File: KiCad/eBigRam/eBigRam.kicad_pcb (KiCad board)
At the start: 2 copper layers, 101.6 x 50.8 mm, 8 parts, among them J1 Conn_02x20_Counter_Clockwise_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

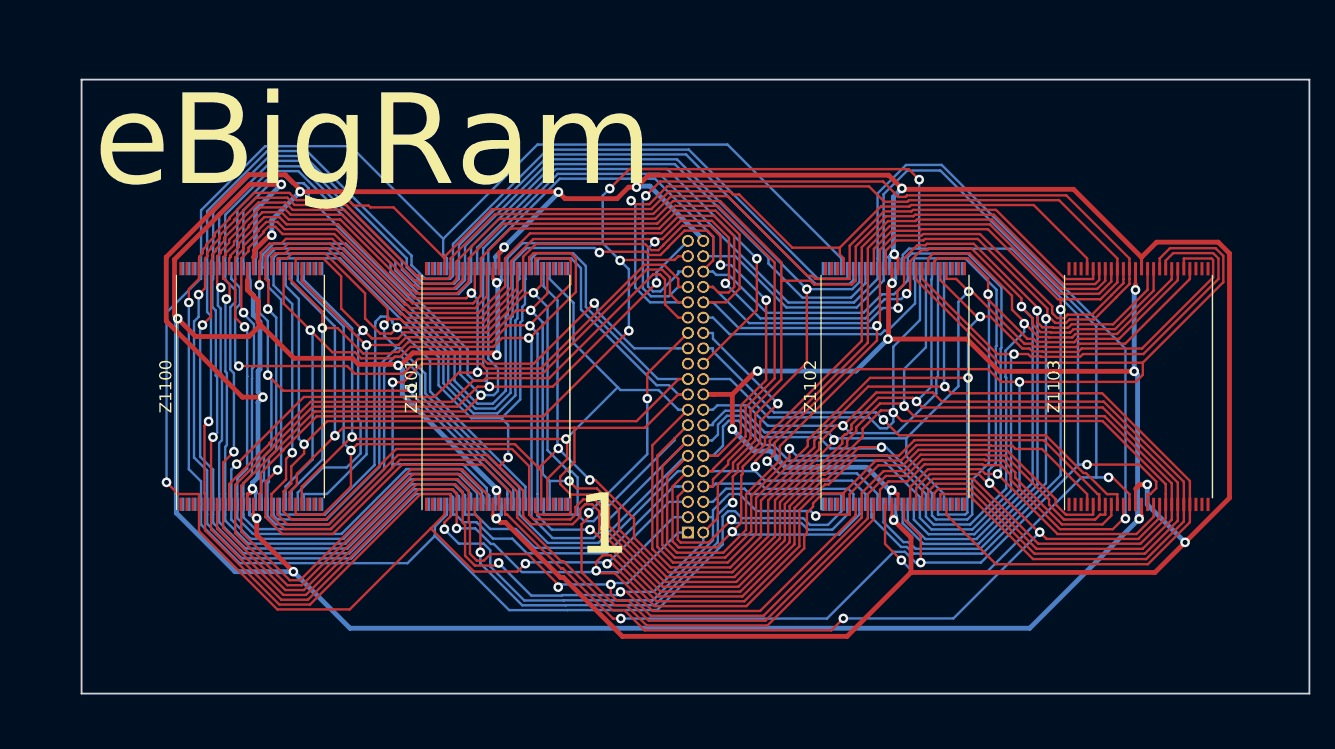
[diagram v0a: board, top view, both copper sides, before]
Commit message: Add some outline designs for add on cards and adapters. Modify ACEeZ80 so that full address bus is on the expander slot, add I2C pins
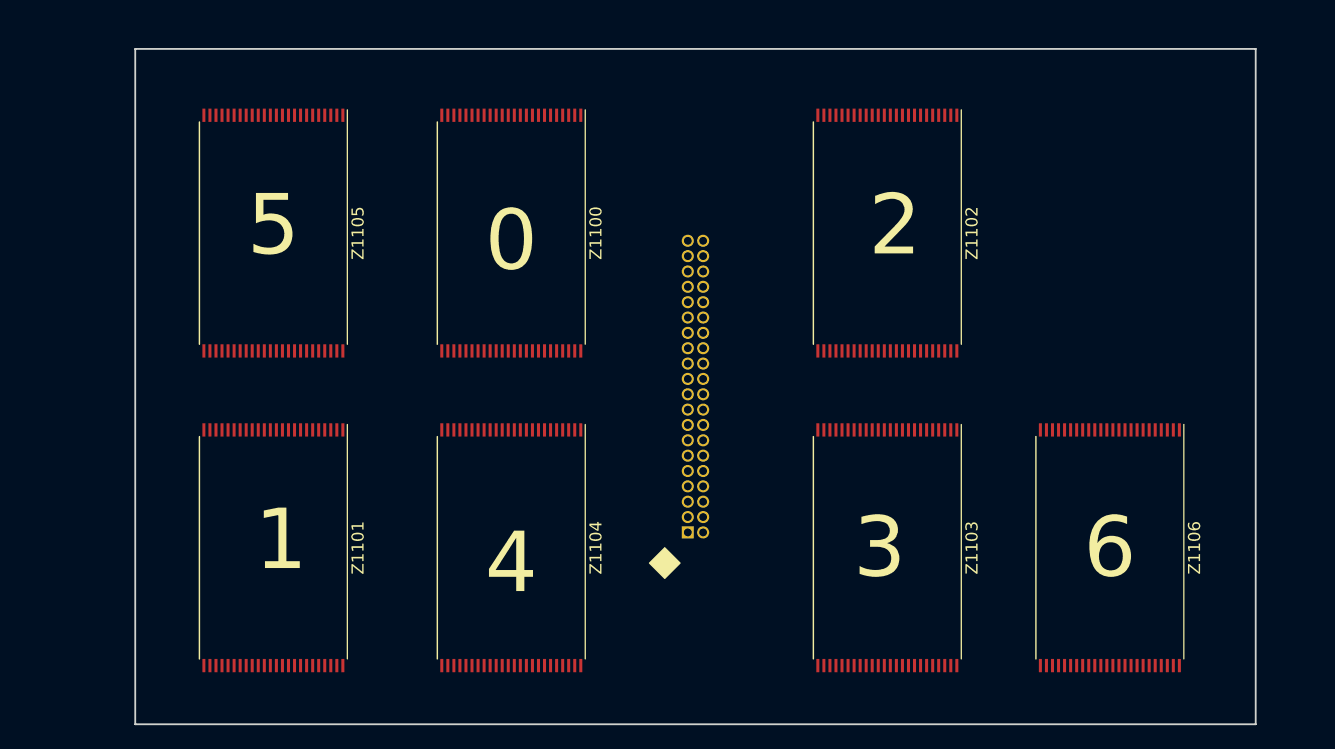
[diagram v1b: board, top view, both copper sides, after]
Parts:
- Z1104, Z1105: moved to F.Cu
- Z1106: value Z1106 -> AS7C316096A-10TIN; moved to F.Cu
- moved Z1104 25.2 mm to (92.7, 70.5)
- moved Z1100 25.0 mm to (92.7, 44.5), turned to 270 degrees
- moved Z1103 24.7 mm to (123.8, 70.5), turned to 270 degrees
- moved Z1101 22.7 mm to (73.0, 70.5), turned to 270 degrees
- moved Z1105 22.5 mm to (73.0, 44.5)
- moved Z1106 22.4 mm to (142.2, 70.5)
- moved Z1102 12.7 mm to (123.8, 44.5), turned to 270 degrees
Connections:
- Z1106 pad 9: Net-(Z1106-Pad9) -> /~15&16Meg
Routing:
- net GND: track 284.9 -> 0.00 mm, vias 16 -> 0
- net VCC: track 278.5 -> 0.00 mm, vias 13 -> 0
- net /DA0: track 240.8 -> 0.00 mm, vias 3 -> 0
- net /DA2: track 240.6 -> 0.00 mm, vias 7 -> 0
- net /A2: track 231.3 -> 0.00 mm, vias 3 -> 0
- net /~RD: track 228.4 -> 0.00 mm, vias 5 -> 0
- net /DA6: track 227.2 -> 0.00 mm, vias 4 -> 0
- net /DA1: track 217.5 -> 0.00 mm, vias 3 -> 0
- net /A19: track 212.7 -> 0.00 mm, vias 2 -> 0
- net /~WR: track 211.0 -> 0.00 mm, vias 4 -> 0
- net /A1: track 208.8 -> 0.00 mm, vias 3 -> 0
- net /A10: track 208.3 -> 0.00 mm, vias 2 -> 0
- net /A0: track 206.2 -> 0.00 mm, vias 3 -> 0
- net /A4: track 203.1 -> 0.00 mm, vias 3 -> 0
- net /A20: track 199.2 -> 0.00 mm, vias 2 -> 0
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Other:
- board size 101.6 x 50.8 mm -> 92.7 x 55.9 mm
- net class Default: clearance 0.2 -> 0.15; via_dia 0.8 -> 0.6
- net class PWR: clearance 0.2 -> 0.15; via_dia 0.8 -> 0.6
- rule trace_clearance: 0.2 -> 0.15
- board text added: "0"
- board text added: "2"
- board text added: "3"
- board text added: "4"
- board text added: "5"
- board text added: "6"

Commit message: Add example to UniBoard. Correct power and bus routing on ACEeZ80.jpg
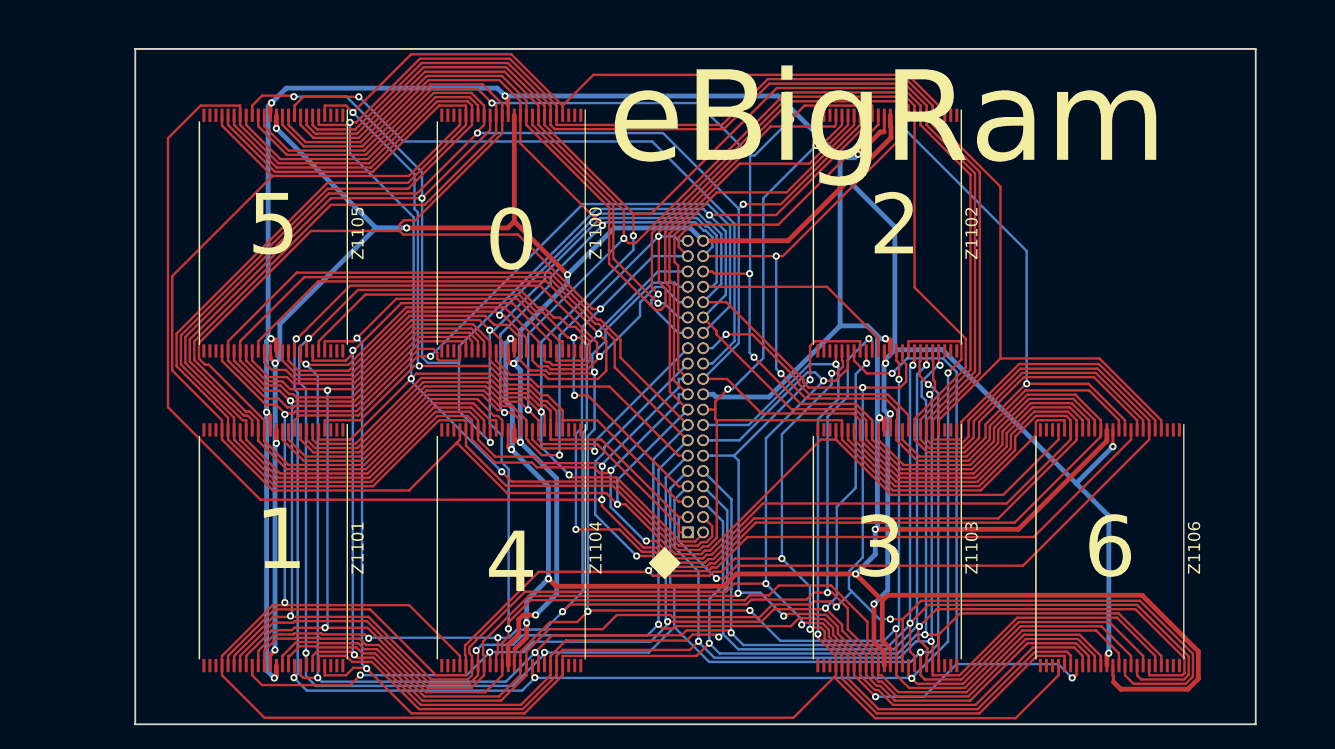
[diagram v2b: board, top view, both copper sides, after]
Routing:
- net GND: track 0.00 -> 296.6 mm, vias 0 -> 14
- net /A19: track 0.00 -> 248.3 mm, vias 0 -> 2
- net VCC: track 0.00 -> 243.8 mm, vias 0 -> 15
- net /DA2: track 0.00 -> 239.2 mm, vias 0 -> 2
- net /A18: track 0.00 -> 220.7 mm, vias 0 -> 2
- net /A12: track 0.00 -> 206.9 mm, vias 0 -> 5
- net /A2: track 0.00 -> 203.9 mm, vias 0 -> 1
- net /A3: track 0.00 -> 197.0 mm, vias 0 -> 3
- net /A14: track 0.00 -> 196.9 mm, vias 0 -> 4
- net /A17: track 0.00 -> 194.8 mm, vias 0 -> 2
- net /DA7: track 0.00 -> 193.2 mm, vias 0 -> 4
- net /~RD: track 0.00 -> 189.5 mm, vias 0 -> 6
- net /DA4: track 0.00 -> 188.5 mm, vias 0 -> 6
- net /DA3: track 0.00 -> 187.8 mm, vias 0 -> 4
- net /A20: track 0.00 -> 186.4 mm, vias 0 -> 2
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
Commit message: First complete system. Unlikely to work but will serve as the basis of a system to test VGA.
Signed-off-by: John Bradley <flypie@rocketmail.com>
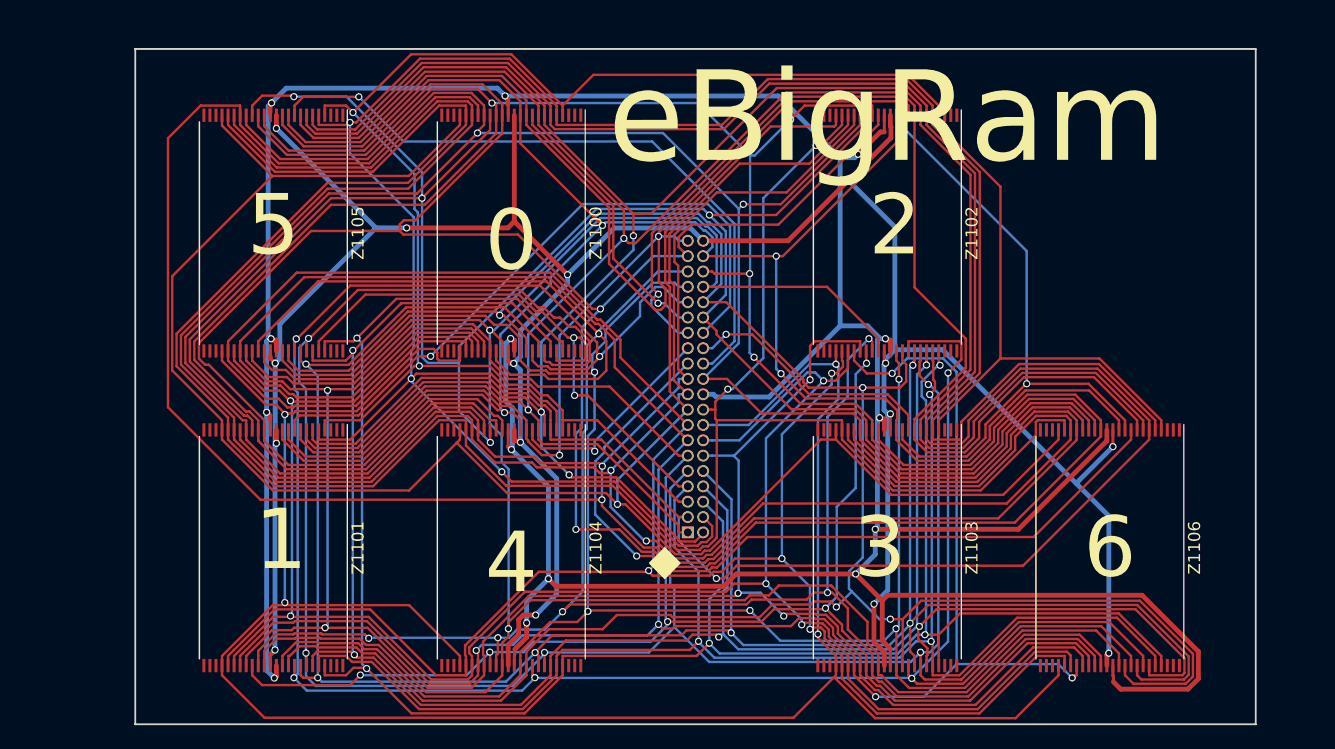
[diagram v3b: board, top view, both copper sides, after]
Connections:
- net /~11&12Meg renamed /~{11&12Meg}
- net /~13&14Meg renamed /~{13&14Meg}
- net /~15&16Meg renamed /~{15&16Meg}
- net /~3&4Meg renamed /~{3&4Meg}
- net /~5&6Meg renamed /~{5&6Meg}
- net /~7&8Meg renamed /~{7&8Meg}
- net /~9&10Meg renamed /~{9&10Meg}
- net /~RD renamed /~{RD}
- net /~WR renamed /~{WR}
- Z1100 pad 1: Net-(Z1100-Pad1) -> unconnected-(Z1100-Pad1)
- Z1100 pad 2: Net-(Z1100-Pad2) -> unconnected-(Z1100-Pad2)
- Z1100 pad 22: Net-(Z1100-Pad22) -> unconnected-(Z1100-Pad22)
- Z1100 pad 23: Net-(Z1100-Pad23) -> unconnected-(Z1100-Pad23)
- Z1100 pad 24: Net-(Z1100-Pad24) -> unconnected-(Z1100-Pad24)
- Z1100 pad 25: Net-(Z1100-Pad25) -> unconnected-(Z1100-Pad25)
- Z1100 pad 26: Net-(Z1100-Pad26) -> unconnected-(Z1100-Pad26)
- Z1100 pad 27: Net-(Z1100-Pad27) -> unconnected-(Z1100-Pad27)
- Z1100 pad 3: Net-(Z1100-Pad3) -> unconnected-(Z1100-Pad3)
- Z1100 pad 46: Net-(Z1100-Pad46) -> unconnected-(Z1100-Pad46)
- Z1100 pad 47: Net-(Z1100-Pad47) -> unconnected-(Z1100-Pad47)
- Z1100 pad 48: Net-(Z1100-Pad48) -> unconnected-(Z1100-Pad48)
- Z1101 pad 1: Net-(Z1101-Pad1) -> unconnected-(Z1101-Pad1)
- Z1101 pad 2: Net-(Z1101-Pad2) -> unconnected-(Z1101-Pad2)
- Z1101 pad 22: Net-(Z1101-Pad22) -> unconnected-(Z1101-Pad22)
- Z1101 pad 23: Net-(Z1101-Pad23) -> unconnected-(Z1101-Pad23)
- Z1101 pad 24: Net-(Z1101-Pad24) -> unconnected-(Z1101-Pad24)
- Z1101 pad 25: Net-(Z1101-Pad25) -> unconnected-(Z1101-Pad25)
- Z1101 pad 26: Net-(Z1101-Pad26) -> unconnected-(Z1101-Pad26)
- Z1101 pad 27: Net-(Z1101-Pad27) -> unconnected-(Z1101-Pad27)
- Z1101 pad 3: Net-(Z1101-Pad3) -> unconnected-(Z1101-Pad3)
- Z1101 pad 46: Net-(Z1101-Pad46) -> unconnected-(Z1101-Pad46)
- Z1101 pad 47: Net-(Z1101-Pad47) -> unconnected-(Z1101-Pad47)
- Z1101 pad 48: Net-(Z1101-Pad48) -> unconnected-(Z1101-Pad48)
- Z1102 pad 1: Net-(Z1102-Pad1) -> unconnected-(Z1102-Pad1)
- Z1102 pad 2: Net-(Z1102-Pad2) -> unconnected-(Z1102-Pad2)
- Z1102 pad 22: Net-(Z1102-Pad22) -> unconnected-(Z1102-Pad22)
- Z1102 pad 23: Net-(Z1102-Pad23) -> unconnected-(Z1102-Pad23)
- Z1102 pad 24: Net-(Z1102-Pad24) -> unconnected-(Z1102-Pad24)
- Z1102 pad 25: Net-(Z1102-Pad25) -> unconnected-(Z1102-Pad25)
- Z1102 pad 26: Net-(Z1102-Pad26) -> unconnected-(Z1102-Pad26)
- Z1102 pad 27: Net-(Z1102-Pad27) -> unconnected-(Z1102-Pad27)
- Z1102 pad 3: Net-(Z1102-Pad3) -> unconnected-(Z1102-Pad3)
- Z1102 pad 46: Net-(Z1102-Pad46) -> unconnected-(Z1102-Pad46)
- Z1102 pad 47: Net-(Z1102-Pad47) -> unconnected-(Z1102-Pad47)
- Z1102 pad 48: Net-(Z1102-Pad48) -> unconnected-(Z1102-Pad48)
- Z1103 pad 1: Net-(Z1103-Pad1) -> unconnected-(Z1103-Pad1)
- Z1103 pad 2: Net-(Z1103-Pad2) -> unconnected-(Z1103-Pad2)
- Z1103 pad 22: Net-(Z1103-Pad22) -> unconnected-(Z1103-Pad22)
- Z1103 pad 23: Net-(Z1103-Pad23) -> unconnected-(Z1103-Pad23)
- Z1103 pad 24: Net-(Z1103-Pad24) -> unconnected-(Z1103-Pad24)
- Z1103 pad 25: Net-(Z1103-Pad25) -> unconnected-(Z1103-Pad25)
- Z1103 pad 26: Net-(Z1103-Pad26) -> unconnected-(Z1103-Pad26)
- Z1103 pad 27: Net-(Z1103-Pad27) -> unconnected-(Z1103-Pad27)
- Z1103 pad 3: Net-(Z1103-Pad3) -> unconnected-(Z1103-Pad3)
- Z1103 pad 46: Net-(Z1103-Pad46) -> unconnected-(Z1103-Pad46)
- Z1103 pad 47: Net-(Z1103-Pad47) -> unconnected-(Z1103-Pad47)
- Z1103 pad 48: Net-(Z1103-Pad48) -> unconnected-(Z1103-Pad48)
- Z1104 pad 1: Net-(Z1104-Pad1) -> unconnected-(Z1104-Pad1)
- Z1104 pad 2: Net-(Z1104-Pad2) -> unconnected-(Z1104-Pad2)
- Z1104 pad 22: Net-(Z1104-Pad22) -> unconnected-(Z1104-Pad22)
- Z1104 pad 23: Net-(Z1104-Pad23) -> unconnected-(Z1104-Pad23)
- Z1104 pad 24: Net-(Z1104-Pad24) -> unconnected-(Z1104-Pad24)
- Z1104 pad 25: Net-(Z1104-Pad25) -> unconnected-(Z1104-Pad25)
- Z1104 pad 26: Net-(Z1104-Pad26) -> unconnected-(Z1104-Pad26)
- Z1104 pad 27: Net-(Z1104-Pad27) -> unconnected-(Z1104-Pad27)
- Z1104 pad 3: Net-(Z1104-Pad3) -> unconnected-(Z1104-Pad3)
- Z1104 pad 46: Net-(Z1104-Pad46) -> unconnected-(Z1104-Pad46)
- Z1104 pad 47: Net-(Z1104-Pad47) -> unconnected-(Z1104-Pad47)
- Z1104 pad 48: Net-(Z1104-Pad48) -> unconnected-(Z1104-Pad48)
- Z1105 pad 1: Net-(Z1105-Pad1) -> unconnected-(Z1105-Pad1)
- Z1105 pad 2: Net-(Z1105-Pad2) -> unconnected-(Z1105-Pad2)
- Z1105 pad 22: Net-(Z1105-Pad22) -> unconnected-(Z1105-Pad22)
- Z1105 pad 23: Net-(Z1105-Pad23) -> unconnected-(Z1105-Pad23)
- Z1105 pad 24: Net-(Z1105-Pad24) -> unconnected-(Z1105-Pad24)
- Z1105 pad 25: Net-(Z1105-Pad25) -> unconnected-(Z1105-Pad25)
- Z1105 pad 26: Net-(Z1105-Pad26) -> unconnected-(Z1105-Pad26)
- Z1105 pad 27: Net-(Z1105-Pad27) -> unconnected-(Z1105-Pad27)
- Z1105 pad 3: Net-(Z1105-Pad3) -> unconnected-(Z1105-Pad3)
- Z1105 pad 46: Net-(Z1105-Pad46) -> unconnected-(Z1105-Pad46)
- Z1105 pad 47: Net-(Z1105-Pad47) -> unconnected-(Z1105-Pad47)
- Z1105 pad 48: Net-(Z1105-Pad48) -> unconnected-(Z1105-Pad48)
- Z1106 pad 1: Net-(Z1106-Pad1) -> unconnected-(Z1106-Pad1)
- Z1106 pad 2: Net-(Z1106-Pad2) -> unconnected-(Z1106-Pad2)
- Z1106 pad 22: Net-(Z1106-Pad22) -> unconnected-(Z1106-Pad22)
- Z1106 pad 23: Net-(Z1106-Pad23) -> unconnected-(Z1106-Pad23)
- Z1106 pad 24: Net-(Z1106-Pad24) -> unconnected-(Z1106-Pad24)
- Z1106 pad 25: Net-(Z1106-Pad25) -> unconnected-(Z1106-Pad25)
- Z1106 pad 26: Net-(Z1106-Pad26) -> unconnected-(Z1106-Pad26)
- Z1106 pad 27: Net-(Z1106-Pad27) -> unconnected-(Z1106-Pad27)
- Z1106 pad 3: Net-(Z1106-Pad3) -> unconnected-(Z1106-Pad3)
- Z1106 pad 46: Net-(Z1106-Pad46) -> unconnected-(Z1106-Pad46)
- Z1106 pad 47: Net-(Z1106-Pad47) -> unconnected-(Z1106-Pad47)
- Z1106 pad 48: Net-(Z1106-Pad48) -> unconnected-(Z1106-Pad48)
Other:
- net class Default removed
- net class PWR removed
